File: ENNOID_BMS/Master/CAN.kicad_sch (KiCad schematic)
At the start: 8 parts, among them U8 ISO1050DUBR, U9 SFH617A-2X009T

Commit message: ENNOID BMS PCBs completed
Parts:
- D4: footprint TO_SOT_Packages_SMD:SOT-23 -> Package_TO_SOT_SMD:SOT-23
- U9: footprint Housings_DIP:SMDIP-4_W9.53mm_Clearance8mm -> Package_DIP:SMDIP-4_W9.53mm_Clearance8mm
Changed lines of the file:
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@@
 			)
 		)
-		(property "Footprint" "TO_SOT_Packages_SMD:SOT-23"
+		(property "Footprint" "Package_TO_SOT_SMD:SOT-23"
 			(at 183.515 100.33 0)
 			(effects
@@
 			)
 		)
-		(property "Footprint" "Housings_DIP:SMDIP-4_W9.53mm_Clearance8mm"
+		(property "Footprint" "Package_DIP:SMDIP-4_W9.53mm_Clearance8mm"
 			(at 142.24 163.83 0)
 			(effects

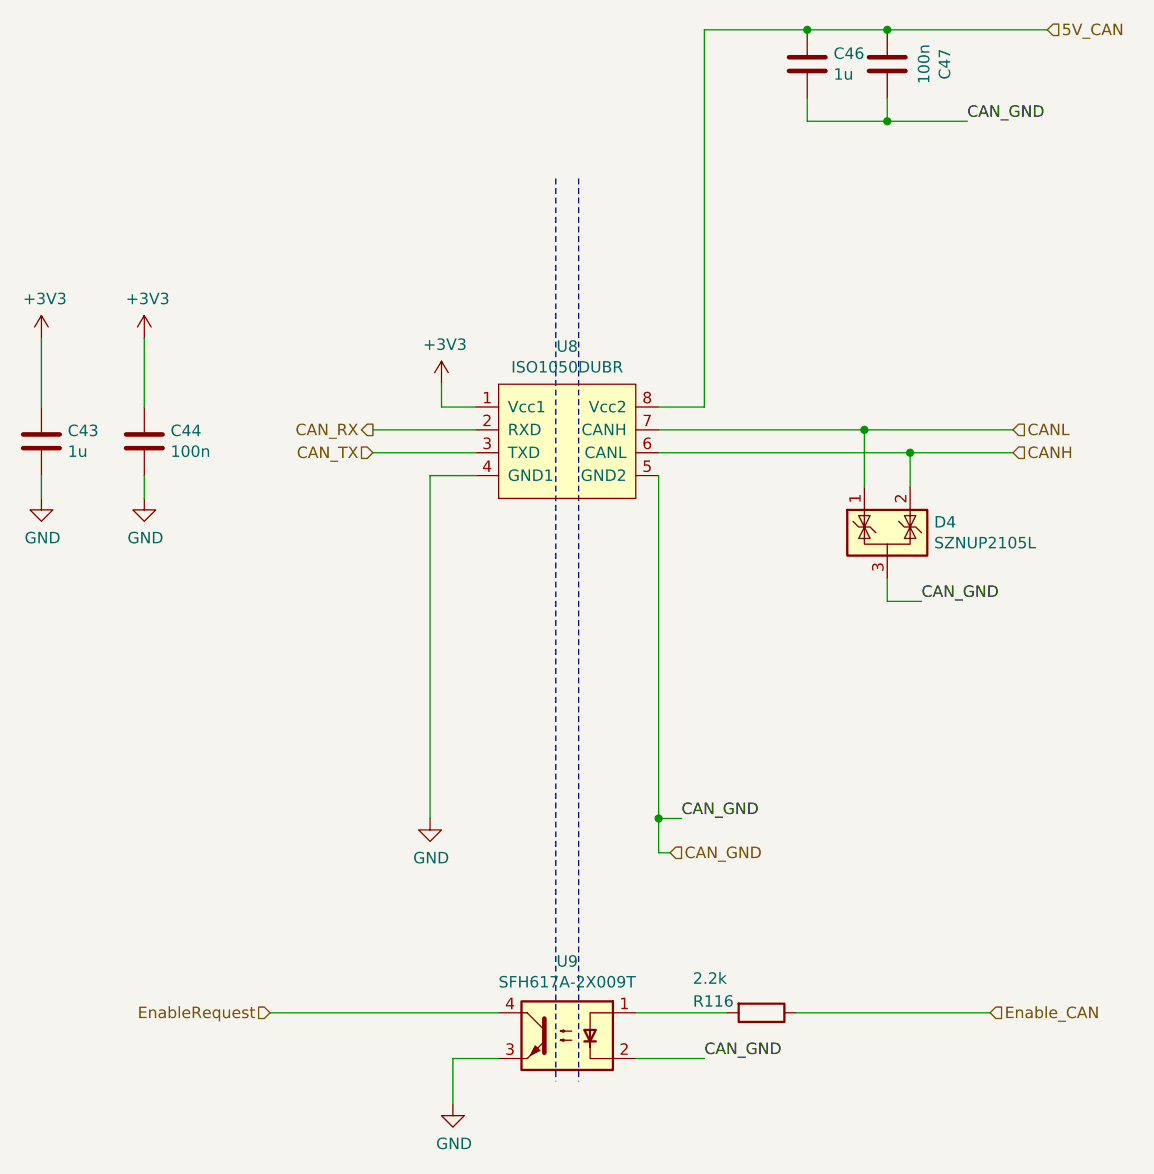
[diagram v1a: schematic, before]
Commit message: Slave with SMD and no other fuses
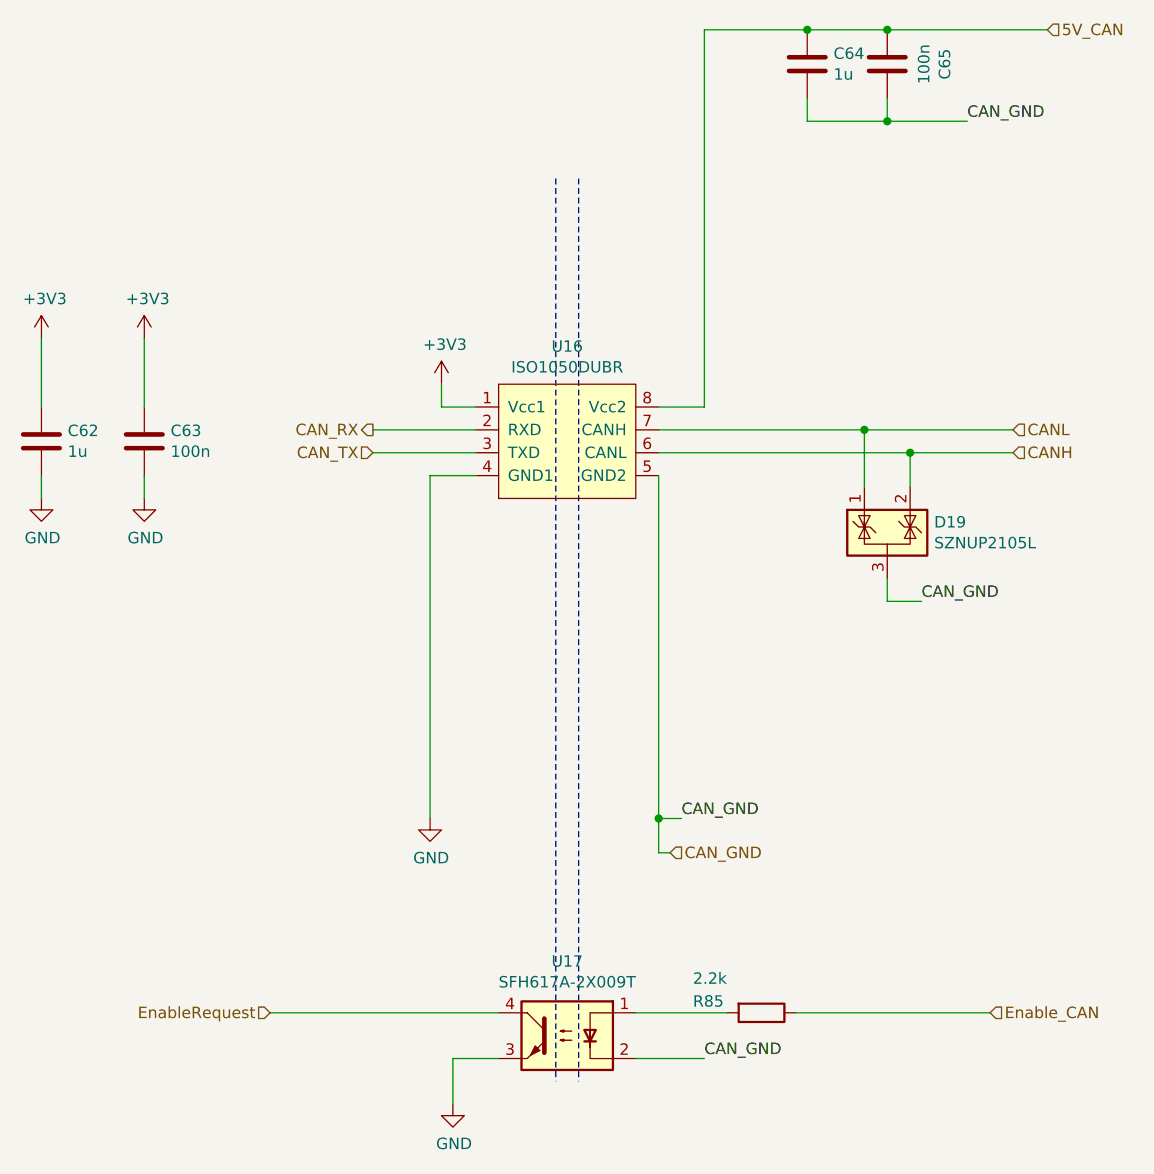
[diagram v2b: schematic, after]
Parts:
- renumbered C43 to C62, C44 to C63, C46 to C64, C47 to C65, D4 to D19, R116 to R85, U8 to U16, U9 to U17
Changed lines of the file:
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@@
 		(on_board yes)
 		(dnp no)
-		(property "Reference" "U8"
+		(property "Reference" "U16"
 			(at 142.24 78.359 0)
 			(effects
@@
 			)
 		)
-		(property "Datasheet" ""
+		(property "Datasheet" "https://www.ti.com/lit/gpn/iso1050"
 			(at 139.7 97.79 0)
 			(effects
@@
 			(project "BMS-Master"
 				(path "/b08f1666-8d98-49de-9988-f6179a2f79fe/00000000-0000-0000-0000-00005a91e16c"
-					(reference "U8")
+					(reference "U16")
 					(unit 1)
 				)
@@
 		(on_board yes)
 		(dnp no)
-		(property "Reference" "#PWR0183"
+		(property "Reference" "#PWR0122"
 			(at 128.27 86.36 0)
 			(effects
@@
 				)
 				(path "/b08f1666-8d98-49de-9988-f6179a2f79fe/00000000-0000-0000-0000-00005a91e16c"
-					(reference "#PWR0183")
+					(reference "#PWR0122")
 					(unit 1)
 				)
@@
 		(on_board yes)
 		(dnp no)
-		(property "Reference" "#PWR0184"
+		(property "Reference" "#PWR0121"
 			(at 127 137.16 0)
 			(effects
@@
 			(project "BMS-Master"
 				(path "/b08f1666-8d98-49de-9988-f6179a2f79fe/00000000-0000-0000-0000-00005a91e16c"
-					(reference "#PWR0184")
+					(reference "#PWR0121")
 					(unit 1)
 				)
@@
 		(on_board yes)
 		(dnp no)
-		(property "Reference" "C44"
+		(property "Reference" "C63"
 			(at 98.171 87.7316 0)
 			(effects
@@
 			)
 		)
-		(property "Datasheet" "~"
+		(property "Datasheet" "https://search.murata.co.jp/Ceramy/image/img/A01X/G101/ENG/GRM188R71E104KA01-01.pdf"
 			(at 95.25 88.9 0)
 			(effects
@@
 			(project "BMS-Master"
 				(path "/b08f1666-8d98-49de-9988-f6179a2f79fe/00000000-0000-0000-0000-00005a91e16c"
-					(reference "C44")
+					(reference "C63")
 					(unit 1)
 				)
@@
 		(on_board yes)
 		(dnp no)
-		(property "Reference" "#PWR0185"
+		(property "Reference" "#PWR0119"
 			(at 95.25 81.28 0)
 			(effects
@@
 				)
 				(path "/b08f1666-8d98-49de-9988-f6179a2f79fe/00000000-0000-0000-0000-00005a91e16c"
-					(reference "#PWR0185")
+					(reference "#PWR0119")
 					(unit 1)
 				)
@@
 		(on_board yes)
 		(dnp no)
-		(property "Reference" "#PWR0186"
+		(property "Reference" "#PWR0120"
 			(at 95.25 101.6 0)
 			(effects
@@
 			(project "BMS-Master"
 				(path "/b08f1666-8d98-49de-9988-f6179a2f79fe/00000000-0000-0000-0000-00005a91e16c"
-					(reference "#PWR0186")
+					(reference "#PWR0120")
 					(unit 1)
 				)
@@
 		(on_board yes)
 		(dnp no)
-		(property "Reference" "C43"
+		(property "Reference" "C62"
 			(at 86.741 87.7316 0)
 			(effects
@@
 			)
 		)
-		(property "Datasheet" "~"
+		(property "Datasheet" "https://search.murata.co.jp/Ceramy/image/img/A01X/G101/ENG/GRM188R71E105KA12-01.pdf"
 			(at 83.82 88.9 0)
 			(effects
@@
 			(project "BMS-Master"
 				(path "/b08f1666-8d98-49de-9988-f6179a2f79fe/00000000-0000-0000-0000-00005a91e16c"
-					(reference "C43")
+					(reference "C62")
 					(unit 1)
 				)
@@
 		(on_board yes)
 		(dnp no)
-		(property "Reference" "#PWR0187"
+		(property "Reference" "#PWR0117"
 			(at 83.82 81.28 0)
 			(effects
@@
 				)
 				(path "/b08f1666-8d98-49de-9988-f6179a2f79fe/00000000-0000-0000-0000-00005a91e16c"
-					(reference "#PWR0187")
+					(reference "#PWR0117")
 					(unit 1)
 				)
@@
 		(on_board yes)
 		(dnp no)
-		(property "Reference" "#PWR0188"
+		(property "Reference" "#PWR0118"
 			(at 83.82 101.6 0)
 			(effects
@@
 			(project "BMS-Master"
 				(path "/b08f1666-8d98-49de-9988-f6179a2f79fe/00000000-0000-0000-0000-00005a91e16c"
-					(reference "#PWR0188")
+					(reference "#PWR0118")
 					(unit 1)
 				)
@@
 		(on_board yes)
 		(dnp no)
-		(property "Reference" "C47"
+		(property "Reference" "C65"
 			(at 184.2008 46.99 90)
 			(effects
@@
 			)
 		)
-		(property "Datasheet" "~"
+		(property "Datasheet" "https://search.murata.co.jp/Ceramy/image/img/A01X/G101/ENG/GRM188R71E104KA01-01.pdf"
 			(at 177.8 46.99 0)
 			(effects
@@
 			(project "BMS-Master"
 				(path "/b08f1666-8d98-49de-9988-f6179a2f79fe/00000000-0000-0000-0000-00005a91e16c"
-					(reference "C47")
+					(reference "C65")
 					(unit 1)
 				)
@@
 		(on_board yes)
 		(dnp no)
-		(property "Reference" "C46"
+		(property "Reference" "C64"
 			(at 171.831 45.8216 0)
 			(effects
@@
 			)
 		)
-		(property "Datasheet" "~"
+		(property "Datasheet" "https://search.murata.co.jp/Ceramy/image/img/A01X/G101/ENG/GRM188R71E105KA12-01.pdf"
 			(at 168.91 46.99 0)
 			(effects
@@
 			(project "BMS-Master"
 				(path "/b08f1666-8d98-49de-9988-f6179a2f79fe/00000000-0000-0000-0000-00005a91e16c"
-					(reference "C46")
+					(reference "C64")
 					(unit 1)
 				)
@@
 		(on_board yes)
 		(dnp no)
-		(property "Reference" "D4"
+		(property "Reference" "D19"
 			(at 183.007 97.8916 0)
 			(effects
@@
 			(project "BMS-Master"
 				(path "/b08f1666-8d98-49de-9988-f6179a2f79fe/00000000-0000-0000-0000-00005a91e16c"
-					(reference "D4")
+					(reference "D19")
 					(unit 1)
 				)
@@
 		(on_board yes)
 		(dnp no)
-		(property "Reference" "U9"
+		(property "Reference" "U17"
 			(at 142.24 146.685 0)
 			(effects
@@
 			(project "BMS-Master"
 				(path "/b08f1666-8d98-49de-9988-f6179a2f79fe/00000000-0000-0000-0000-00005a91e16c"
-					(reference "U9")
+					(reference "U17")
 					(unit 1)
 				)
@@
 		(on_board yes)
 		(dnp no)
-		(property "Reference" "#PWR0189"
+		(property "Reference" "#PWR0123"
 			(at 129.54 168.91 0)
 			(effects
@@
 			(project "BMS-Master"
 				(path "/b08f1666-8d98-49de-9988-f6179a2f79fe/00000000-0000-0000-0000-00005a91e16c"
-					(reference "#PWR0189")
+					(reference "#PWR0123")
 					(unit 1)
 				)
@@
 		(on_board yes)
 		(dnp no)
-		(property "Reference" "R116"
+		(property "Reference" "R85"
 			(at 156.21 151.13 90)
 			(effects
@@
 			)
 		)
-		(property "Datasheet" "~"
+		(property "Datasheet" "https://www.mouser.com/catalog/specsheets/YAGEO_PYu_RC_Group_51_RoHS_L_12.pdf"
 			(at 163.83 152.4 0)
 			(effects
@@
 			(project "BMS-Master"
 				(path "/b08f1666-8d98-49de-9988-f6179a2f79fe/00000000-0000-0000-0000-00005a91e16c"
-					(reference "R116")
-					(unit 1)
-				)
+					(reference "R85")
+					(unit 1)
+				)
